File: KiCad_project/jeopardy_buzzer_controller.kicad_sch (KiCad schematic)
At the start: 19 parts, among them J1 XLR1, J10 Conn_01x02_Male, J11 TO_ENABLE_SWTICH, J12 TO_ENABLE_LED, J13 TO_POWER_LED, J14 Conn_01x02_Male, J2 XLR2, J3 XLR3, J4 XLR4, J5 XLR5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

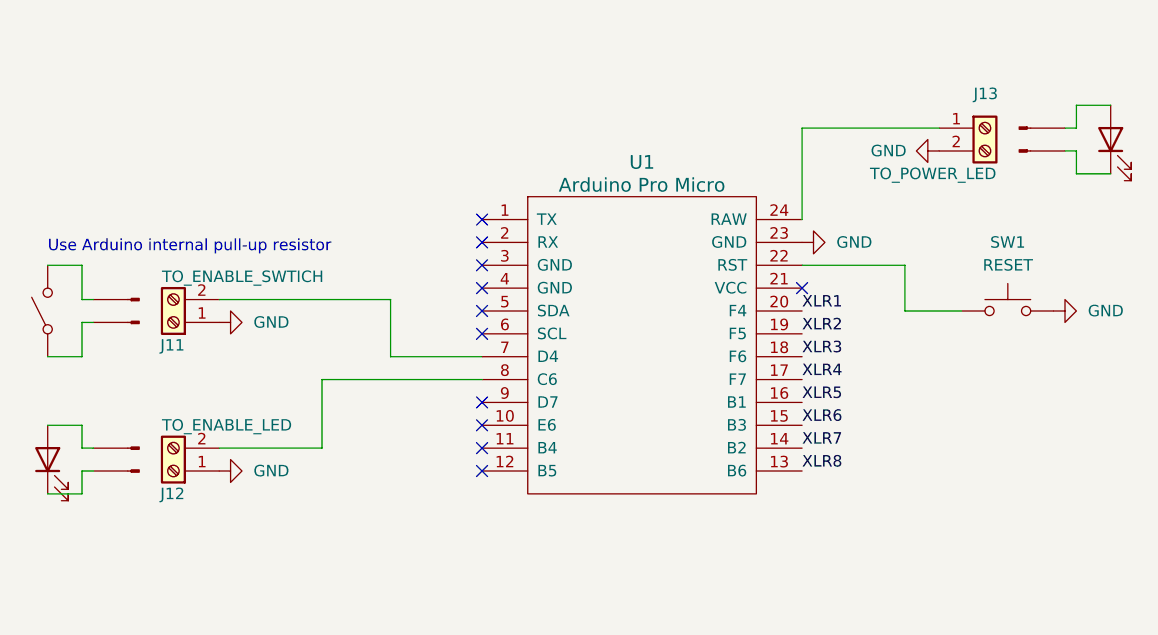
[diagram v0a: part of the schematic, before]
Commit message: Vertically center XLR connectors in downspout
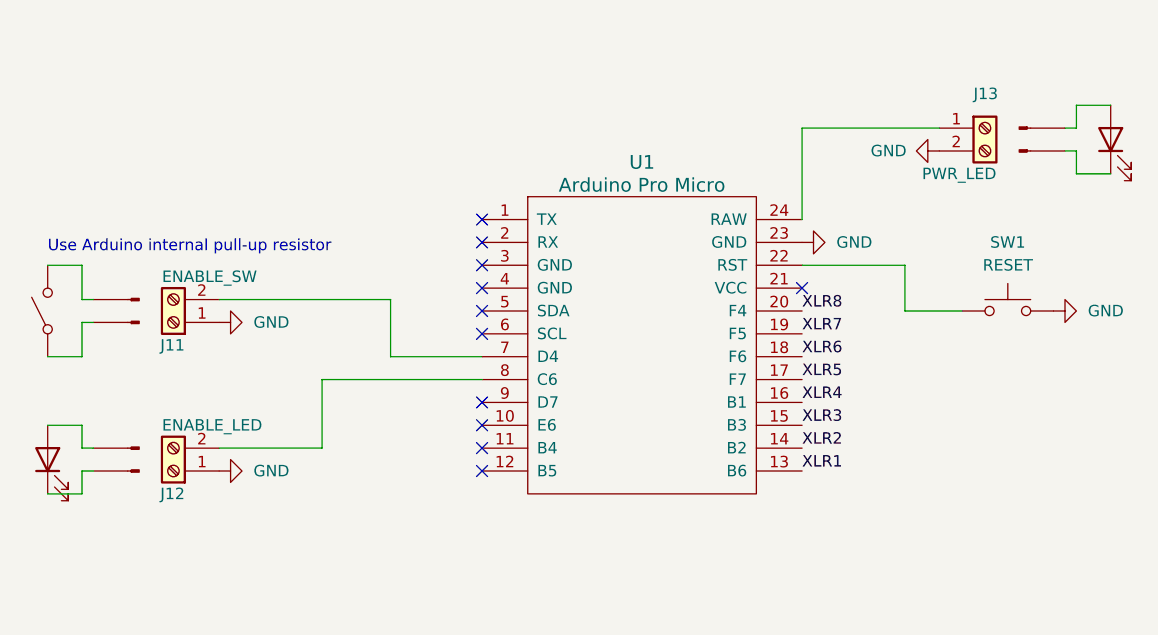
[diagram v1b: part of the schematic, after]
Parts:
- J11: value TO_ENABLE_SWTICH -> ENABLE_SW
- J12: value TO_ENABLE_LED -> ENABLE_LED
- J13: value TO_POWER_LED -> PWR_LED
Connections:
- net XLR1: now also U1.13 (B6); no longer U1.20 (F4)
- net XLR2: now also U1.14 (B2); no longer U1.19 (F5)
- net XLR3: now also U1.15 (B3); no longer U1.18 (F6)
- net XLR4: now also U1.16 (B1); no longer U1.17 (F7)
- net XLR5: now also U1.17 (F7); no longer U1.16 (B1)
- net XLR6: now also U1.18 (F6); no longer U1.15 (B3)
- net XLR7: now also U1.19 (F5); no longer U1.14 (B2)
- net XLR8: now also U1.20 (F4); no longer U1.13 (B6)
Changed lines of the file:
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@@
     (effects (font (size 1.27 1.27)) (justify left bottom))
   )
-  (label "XLR6" (at 120.65 96.52 0)
+  (label "XLR6" (at 120.65 88.9 0)
     (effects (font (size 1.27 1.27)) (justify left bottom))
   )
-  (label "XLR4" (at 120.65 91.44 0)
+  (label "XLR4" (at 120.65 93.98 0)
     (effects (font (size 1.27 1.27)) (justify left bottom))
   )
@@
     (effects (font (size 1.27 1.27)) (justify right bottom))
   )
-  (label "XLR3" (at 120.65 88.9 0)
+  (label "XLR3" (at 120.65 96.52 0)
     (effects (font (size 1.27 1.27)) (justify left bottom))
   )
@@
     (effects (font (size 1.27 1.27)) (justify right bottom))
   )
-  (label "XLR8" (at 120.65 101.6 0)
+  (label "XLR8" (at 120.65 83.82 0)
     (effects (font (size 1.27 1.27)) (justify left bottom))
   )
@@
     (effects (font (size 1.27 1.27)) (justify right bottom))
   )
-  (label "XLR2" (at 120.65 86.36 0)
+  (label "XLR2" (at 120.65 99.06 0)
     (effects (font (size 1.27 1.27)) (justify left bottom))
   )
-  (label "XLR5" (at 120.65 93.98 0)
+  (label "XLR5" (at 120.65 91.44 0)
     (effects (font (size 1.27 1.27)) (justify left bottom))
   )
-  (label "XLR7" (at 120.65 99.06 0)
+  (label "XLR7" (at 120.65 86.36 0)
     (effects (font (size 1.27 1.27)) (justify left bottom))
   )
@@
     (effects (font (size 1.27 1.27)) (justify right bottom))
   )
-  (label "XLR1" (at 120.65 83.82 0)
+  (label "XLR1" (at 120.65 101.6 0)
     (effects (font (size 1.27 1.27)) (justify left bottom))
   )
@@
       (effects (font (size 1.27 1.27)) (justify left))
     )
-    (property "Value" "TO_ENABLE_LED" (id 1) (at 49.53 96.5201 0)
+    (property "Value" "ENABLE_LED" (id 1) (at 49.53 96.5201 0)
       (effects (font (size 1.27 1.27)) (justify right))
     )
@@
       (effects (font (size 1.27 1.27)) (justify left))
     )
-    (property "Value" "TO_POWER_LED" (id 1) (at 142.24 68.5799 0)
+    (property "Value" "PWR_LED" (id 1) (at 142.24 68.5799 0)
       (effects (font (size 1.27 1.27)) (justify right))
     )
@@
       (effects (font (size 1.27 1.27)) (justify left))
     )
-    (property "Value" "TO_ENABLE_SWTICH" (id 1) (at 49.53 80.0101 0)
+    (property "Value" "ENABLE_SW" (id 1) (at 49.53 80.0101 0)
       (effects (font (size 1.27 1.27)) (justify right))
     )
@@
     )
     (path "/90e56cf7-6646-41c9-b84e-95039bf16dbf"
-      (reference "J11") (unit 1) (value "TO_ENABLE_SWTICH") (footprint "TerminalBlock_Phoenix:TerminalBlock_Phoenix_MKDS-1,5-2-5.08_1x02_P5.08mm_Horizontal")
+      (reference "J11") (unit 1) (value "ENABLE_SW") (footprint "TerminalBlock_Phoenix:TerminalBlock_Phoenix_MKDS-1,5-2-5.08_1x02_P5.08mm_Horizontal")
     )
     (path "/2079777d-9cda-4ed0-b86c-5e2aed2d693c"
-      (reference "J12") (unit 1) (value "TO_ENABLE_LED") (footprint "TerminalBlock_Phoenix:TerminalBlock_Phoenix_MKDS-1,5-2-5.08_1x02_P5.08mm_Horizontal")
+      (reference "J12") (unit 1) (value "ENABLE_LED") (footprint "TerminalBlock_Phoenix:TerminalBlock_Phoenix_MKDS-1,5-2-5.08_1x02_P5.08mm_Horizontal")
     )
     (path "/3cb57936-afec-4ffc-9dec-ad1e6ff9acfd"
-      (reference "J13") (unit 1) (value "TO_POWER_LED") (footprint "TerminalBlock_Phoenix:TerminalBlock_Phoenix_MKDS-1,5-2-5.08_1x02_P5.08mm_Horizontal")
+      (reference "J13") (unit 1) (value "PWR_LED") (footprint "TerminalBlock_Phoenix:TerminalBlock_Phoenix_MKDS-1,5-2-5.08_1x02_P5.08mm_Horizontal")
     )
     (path "/16fb7e3b-62f4-461e-a9e1-40ed45123502"

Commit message: Add custom XLR footprint with bigger holes
Adding a modified version of the "Jack_XLR_Neutrik_NC4MBV_Vertical"
footprint included in the KiCad "Connector_Audio" library.

The NC4MBV footprint included with KiCad uses hole sizes specified by
Neutrik here: https://www.neutrik.com/en/product/nc4mbv-1

Pins 1 through 4 are cylindrical, with a double-taper on the tip
and then a shoulder. The ground pin is rectangular with a shoulder only.

The hole sizes specified by Neutrik are for having the pin shoulders
sit on the PCB. They work perfectly for that - the jack can be
pushed into the PCB with a little force, then the pin shoulders hit the
PCB with a satisfying click, and the jack stays held in the PCB by
friction.

But, I want the full diameter of the pins to go through the holes and
the black plastic housing to sit on the PCB.

Changes to the footprint:

* For pads 1 through 4: increase hole size from 1.6mm to 1.95mm.
    * Lead diameter measured with calipers is 1.75mm.
    * Add 0.20mm clearance per https://klc.kicad.org/footprint/f7/f7.6/.

* For pads 1 and 4 only: increase pad size from 3.4mm to 4mm.
     * The PCB will be supported by the XLR connectors so I want a
       strong solder connection.
     * Can't increase pad size on pads 2 and 3 because they're already
       pretty close to each other.

* For the G pad: change shape from circle to oval.
    * The pin is rectangular. The size measured with calipers is
      2.00mm width and 0.50mm height.
    * Per https://klc.kicad.org/footprint/f7/f7.7/:
        * Set the hole height to be the pin height plus 0.20mm.
          0.5mm + 0.2mm = 0.7mm.
        * Set the hole width to be the pin width plus the hole height.
          2mm + 0.7mm = 2.7mm.
    * Make the pad 2mm larger than the hole for strong solder.

* Add more ref texts above and below the pads on both front and back
  silkscreen. Helpful for keeping track of where you are when soldering
  under a microscope.

* TODO: fix silkscreen arc intersecting t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
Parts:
- XLR1: renamed from J1; footprint Connector_Audio:Jack_XLR_Neutrik_NC4MBV_Vertical -> custom_xlr_footprint:Jack_XLR_Neutrik_NC4MBV_Vertical_with_bigger_holes
- XLR2: renamed from J2; footprint Connector_Audio:Jack_XLR_Neutrik_NC4MBV_Vertical -> custom_xlr_footprint:Jack_XLR_Neutrik_NC4MBV_Vertical_with_bigger_holes
- XLR3: renamed from J3; footprint Connector_Audio:Jack_XLR_Neutrik_NC4MBV_Vertical -> custom_xlr_footprint:Jack_XLR_Neutrik_NC4MBV_Vertical_with_bigger_holes
- XLR4: renamed from J4; footprint Connector_Audio:Jack_XLR_Neutrik_NC4MBV_Vertical -> custom_xlr_footprint:Jack_XLR_Neutrik_NC4MBV_Vertical_with_bigger_holes
- XLR5: renamed from J5; footprint Connector_Audio:Jack_XLR_Neutrik_NC4MBV_Vertical -> custom_xlr_footprint:Jack_XLR_Neutrik_NC4MBV_Vertical_with_bigger_holes
- XLR6: renamed from J6; footprint Connector_Audio:Jack_XLR_Neutrik_NC4MBV_Vertical -> custom_xlr_footprint:Jack_XLR_Neutrik_NC4MBV_Vertical_with_bigger_holes
- XLR7: renamed from J7; footprint Connector_Audio:Jack_XLR_Neutrik_NC4MBV_Vertical -> custom_xlr_footprint:Jack_XLR_Neutrik_NC4MBV_Vertical_with_bigger_holes
- XLR8: renamed from J8; footprint Connector_Audio:Jack_XLR_Neutrik_NC4MBV_Vertical -> custom_xlr_footprint:Jack_XLR_Neutrik_NC4MBV_Vertical_with_bigger_holes
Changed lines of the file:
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@@
   )
   (symbol (lib_id "XLR_connector_with_ground_pin:XLR4_Ground") (at 203.2 147.32 0) (unit 1)
-    (in_bom yes) (on_board yes) (fields_autoplaced)
-    (property "Reference" "J4" (id 0) (at 203.2 137.16 0))
-    (property "Value" "XLR4" (id 1) (at 203.2 139.7 0))
-    (property "Footprint" "Connector_Audio:Jack_XLR_Neutrik_NC4MBV_Vertical" (id 2) (at 203.2 147.32 0)
+    (in_bom yes) (on_board yes)
+    (property "Reference" "XLR4" (id 0) (at 203.2 139.7 0))
+    (property "Value" "XLR4" (id 1) (at 203.2 139.7 0)
+      (effects (font (size 1.27 1.27)) hide)
+    )
+    (property "Footprint" "custom_xlr_footprint:Jack_XLR_Neutrik_NC4MBV_Vertical_with_bigger_holes" (id 2) (at 203.2 147.32 0)
       (effects (font (size 1.27 1.27)) hide)
     )
@@
   )
   (symbol (lib_id "XLR_connector_with_ground_pin:XLR4_Ground") (at 203.2 109.22 0) (unit 1)
-    (in_bom yes) (on_board yes) (fields_autoplaced)
-    (property "Reference" "J3" (id 0) (at 203.2 99.06 0))
-    (property "Value" "XLR3" (id 1) (at 203.2 101.6 0))
-    (property "Footprint" "Connector_Audio:Jack_XLR_Neutrik_NC4MBV_Vertical" (id 2) (at 203.2 109.22 0)
+    (in_bom yes) (on_board yes)
+    (property "Reference" "XLR3" (id 0) (at 203.2 101.6 0))
+    (property "Value" "XLR3" (id 1) (at 203.2 101.6 0)
+      (effects (font (size 1.27 1.27)) hide)
+    )
+    (property "Footprint" "custom_xlr_footprint:Jack_XLR_Neutrik_NC4MBV_Vertical_with_bigger_holes" (id 2) (at 203.2 109.22 0)
       (effects (font (size 1.27 1.27)) hide)
     )
@@
   )
   (symbol (lib_id "XLR_connector_with_ground_pin:XLR4_Ground") (at 241.3 109.22 0) (unit 1)
-    (in_bom yes) (on_board yes) (fields_autoplaced)
-    (property "Reference" "J7" (id 0) (at 241.3 99.06 0))
-    (property "Value" "XLR7" (id 1) (at 241.3 101.6 0))
-    (property "Footprint" "Connector_Audio:Jack_XLR_Neutrik_NC4MBV_Vertical" (id 2) (at 241.3 109.22 0)
+    (in_bom yes) (on_board yes)
+    (property "Reference" "XLR7" (id 0) (at 241.3 101.6 0))
+    (property "Value" "XLR7" (id 1) (at 241.3 101.6 0)
+      (effects (font (size 1.27 1.27)) hide)
+    )
+    (property "Footprint" "custom_xlr_footprint:Jack_XLR_Neutrik_NC4MBV_Vertical_with_bigger_holes" (id 2) (at 241.3 109.22 0)
       (effects (font (size 1.27 1.27)) hide)
     )
@@
   )
   (symbol (lib_id "XLR_connector_with_ground_pin:XLR4_Ground") (at 241.3 71.12 0) (unit 1)
-    (in_bom yes) (on_board yes) (fields_autoplaced)
-    (property "Reference" "J6" (id 0) (at 241.3 60.96 0))
-    (property "Value" "XLR6" (id 1) (at 241.3 63.5 0))
-    (property "Footprint" "Connector_Audio:Jack_XLR_Neutrik_NC4MBV_Vertical" (id 2) (at 241.3 71.12 0)
+    (in_bom yes) (on_board yes)
+    (property "Reference" "XLR6" (id 0) (at 241.3 63.5 0))
+    (property "Value" "XLR6" (id 1) (at 241.3 63.5 0)
+      (effects (font (size 1.27 1.27)) hide)
+    )
+    (property "Footprint" "custom_xlr_footprint:Jack_XLR_Neutrik_NC4MBV_Vertical_with_bigger_holes" (id 2) (at 241.3 71.12 0)
       (effects (font (size 1.27 1.27)) hide)
     )
@@
   )
   (symbol (lib_id "XLR_connector_with_ground_pin:XLR4_Ground") (at 203.2 71.12 0) (unit 1)
-    (in_bom yes) (on_board yes) (fields_autoplaced)
-    (property "Reference" "J2" (id 0) (at 203.2 60.96 0))
-    (property "Value" "XLR2" (id 1) (at 203.2 63.5 0))
-    (property "Footprint" "Connector_Audio:Jack_XLR_Neutrik_NC4MBV_Vertical" (id 2) (at 203.2 71.12 0)
+    (in_bom yes) (on_board yes)
+    (property "Reference" "XLR2" (id 0) (at 203.2 63.5 0))
+    (property "Value" "XLR2" (id 1) (at 203.2 63.5 0)
+      (effects (font (size 1.27 1.27)) hide)
+    )
+    (property "Footprint" "custom_xlr_footprint:Jack_XLR_Neutrik_NC4MBV_Vertical_with_bigger_holes" (id 2) (at 203.2 71.12 0)
       (effects (font (size 1.27 1.27)) hide)
     )
@@
   )
   (symbol (lib_id "XLR_connector_with_ground_pin:XLR4_Ground") (at 203.2 33.02 0) (unit 1)
-    (in_bom yes) (on_board yes) (fields_autoplaced)
-    (property "Reference" "J1" (id 0) (at 203.2 22.86 0))
-    (property "Value" "XLR1" (id 1) (at 203.2 25.4 0))
-    (property "Footprint" "Connector_Audio:Jack_XLR_Neutrik_NC4MBV_Vertical" (id 2) (at 203.2 33.02 0)
+    (in_bom yes) (on_board yes)
+    (property "Reference" "XLR1" (id 0) (at 203.2 25.4 0))
+    (property "Value" "XLR1" (id 1) (at 203.2 25.4 0)
+      (effects (font (size 1.27 1.27)) hide)
+    )
+    (property "Footprint" "custom_xlr_footprint:Jack_XLR_Neutrik_NC4MBV_Vertical_with_bigger_holes" (id 2) (at 203.2 33.02 0)
       (effects (font (size 1.27 1.27)) hide)
     )
@@
   )
   (symbol (lib_id "XLR_connector_with_ground_pin:XLR4_Ground") (at 241.3 147.32 0) (unit 1)
-    (in_bom yes) (on_board yes) (fields_autoplaced)
-    (property "Reference" "J8" (id 0) (at 241.3 137.16 0))
-    (property "Value" "XLR8" (id 1) (at 241.3 139.7 0))
-    (property "Footprint" "Connector_Audio:Jack_XLR_Neutrik_NC4MBV_Vertical" (id 2) (at 241.3 147.32 0)
+    (in_bom yes) (on_board yes)
+    (property "Reference" "XLR8" (id 0) (at 241.3 139.7 0))
+    (property "Value" "XLR8" (id 1) (at 241.3 139.7 0)
+      (effects (font (size 1.27 1.27)) hide)
+    )
+    (property "Footprint" "custom_xlr_footprint:Jack_XLR_Neutrik_NC4MBV_Vertical_with_bigger_holes" (id 2) (at 241.3 147.32 0)
       (effects (font (size 1.27 1.27)) hide)
     )
@@
   )
   (symbol (lib_id "XLR_connector_with_ground_pin:XLR4_Ground") (at 241.3 33.02 0) (unit 1)
-    (in_bom yes) (on_board yes) (fields_autoplaced)
-    (property "Reference" "J5" (id 0) (at 241.3 22.86 0))
-    (property "Value" "XLR5" (id 1) (at 241.3 25.4 0))
-    (property "Footprint" "Connector_Audio:Jack_XLR_Neutrik_NC4MBV_Vertical" (id 2) (at 241.3 33.02 0)
+    (in_bom yes) (on_board yes)
+    (property "Reference" "XLR5" (id 0) (at 241.3 25.4 0))
+    (property "Value" "XLR5" (id 1) (at 241.3 25.4 0)
+      (effects (font (size 1.27 1.27)) hide)
+    )
+    (property "Footprint" "custom_xlr_footprint:Jack_XLR_Neutrik_NC4MBV_Vertical_with_bigger_holes" (id 2) (at 241.3 33.02 0)
       (effects (font (size 1.27 1.27)) hide)
     )
@@
       (reference "D2") (unit 1) (value "Enable_LED") (footprint "")
     )
-    (path "/893715f0-7fb5-4740-9a5e-9dc6ebf72619"
-      (reference "J1") (unit 1) (value "XLR1") (footprint "Connector_Audio:Jack_XLR_Neutrik_NC4MBV_Vertical")
-    )
-    (path "/73e13000-f325-4e81-8b7a-dc52703eadf7"
-      (reference "J2") (unit 1) (value "XLR2") (footprint "Connector_Audio:Jack_XLR_Neutrik_NC4MBV_Vertical")
-    )
-    (path "/12931524-47e4-40d6-a5b0-f24a4a77fdfe"
-      (reference "J3") (unit 1) (value "XLR3") (footprint "Connector_Audio:Jack_XLR_Neutrik_NC4MBV_Vertical")
-    )
-    (path "/0f7ba53d-daeb-44b9-9e2b-c191a7240c26"
-      (reference "J4") (unit 1) (value "XLR4") (footprint "Connector_Audio:Jack_XLR_Neutrik_NC4MBV_Vertical")
-    )
-    (path "/d3eac113-377d-46f9-8711-4e808f4db4d2"
-      (reference "J5") (unit 1) (value "XLR5") (footprint "Connector_Audio:Jack_XLR_Neutrik_NC4MBV_Vertical")
-    )
-    (path "/4ec96c3d-278a-4f7c-a3df-0ed4ca6cc500"
-      (reference "J6") (unit 1) (value "XLR6") (footprint "Connector_Audio:Jack_XLR_Neutrik_NC4MBV_Vertical")
-    )
-    (path "/3175ca9d-0808-4c64-b086-36312f457e16"
-      (reference "J7") (unit 1) (value "XLR7") (footprint "Connector_Audio:Jack_XLR_Neutrik_NC4MBV_Vertical")
-    )
-    (path "/afec55b5-d62f-4aeb-9b44-33032b57b8e4"
-      (reference "J8") (unit 1) (value "XLR8") (footprint "Connector_Audio:Jack_XLR_Neutrik_NC4MBV_Vertical")
-    )
     (path "/db010d88-4de8-4e37-b991-f56e64b1ed03"
       (reference "J9") (unit 1) (value "Conn_01x02_Male") (footprint "")
@@
       (reference "U1") (unit 1) (value "Arduino Pro Micro") (footprint "Arduino_Pro_Micro:ProMicro")
     )
-  )
+    (path "/893715f0-7fb5-4740-9a5e-9dc6ebf72619"
+      (reference "XLR1") (unit 1) (value "XLR1") (footprint "custom_xlr_footprint:Jack_XLR_Neutrik_NC4MBV_Vertical_with_bigger_holes")
+    )
+    (path "/73e13000-f325-4e81-8b7a-dc52703eadf7"
+      (reference "XLR2") (unit 1) (value "XLR2") (footprint "custom_xlr_footprint:Jack_XLR_Neutrik_NC4MBV_Vertical_with_bigger_holes")
+    )
+    (path "/12931524-47e4-40d6-a5b0-f24a4a77fdfe"
+      (reference "XLR3") (unit 1) (value "XLR3") (footprint "custom_xlr_footprint:Jack_XLR_Neutrik_NC4MBV_Vertical_with_bigger_holes")
+    )
+    (path "/0f7ba53d-daeb-44b9-9e2b-c191a7240c26"
+      (reference "XLR4") (unit 1) (value "XLR4") (footprint "custom_xlr_footprint:Jack_XLR_Neutrik_NC4MBV_Vertical_with_bigger_holes")
+    )
+    (path "/d3eac113-377d-46f9-8711-4e808f4db4d2"
+      (reference "XLR5") (unit 1) (value "XLR5") (footprint "custom_xlr_footprint:Jack_XLR_Neutrik_NC4MBV_Vertical_with_bigger_holes")
+    )
+    (path "/4ec96c3d-278a-4f7c-a3df-0ed4ca6cc500"
+      (reference "XLR6") (unit 1) (value "XLR6") (footprint "custom_xlr_footprint:Jack_XLR_Neutrik_NC4MBV_Vertical_with_bigger_holes")
+    )
+    (path "/3175ca9d-0808-4c64-b086-36312f457e16"
+      (reference "XLR7") (unit 1) (value "XLR7") (footprint "custom_xlr_footprint:Jack_XLR_Neutrik_NC4MBV_Vertical_with_bigger_holes")
+    )
+    (path "/afec55b5-d62f-4aeb-9b44-33032b57b8e4"
+      (reference "XLR8") (unit 1) (value "XLR8") (footprint "custom_xlr_footprint:Jack_XLR_Neutrik_NC4MBV_Vertical_with_bigger_holes")
+    )
+  )
